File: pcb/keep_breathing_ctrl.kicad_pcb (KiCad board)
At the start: 4 copper layers, 112 x 131 mm, 177 parts, among them J2 Screw_Terminal, P1 CONN_RASPBERRY, Q1 PN2222, Q2 PN2222, U1 MPL3115A2, U10 PCF8523TK, U11 AQH3213AX, U12 AQH3213AX, U13 HTS221, U14 ICE40UP5K-SG48ITR, U15 GD25Q32CTIGR-Memory_Flash, U16 UCC12040, U17 ISO7762, U18 ZLDO1117G33TA, U19 NCP177, U2 powerSTEP01, U3 TLP240D, U4 TLP240D, U5 TLP240D, U6 TLP240D, U7 TLP240D, U8 TLP240D, U9 ZLDO1117G33TA, Y1 ABS06-107-32.768KHZ-T

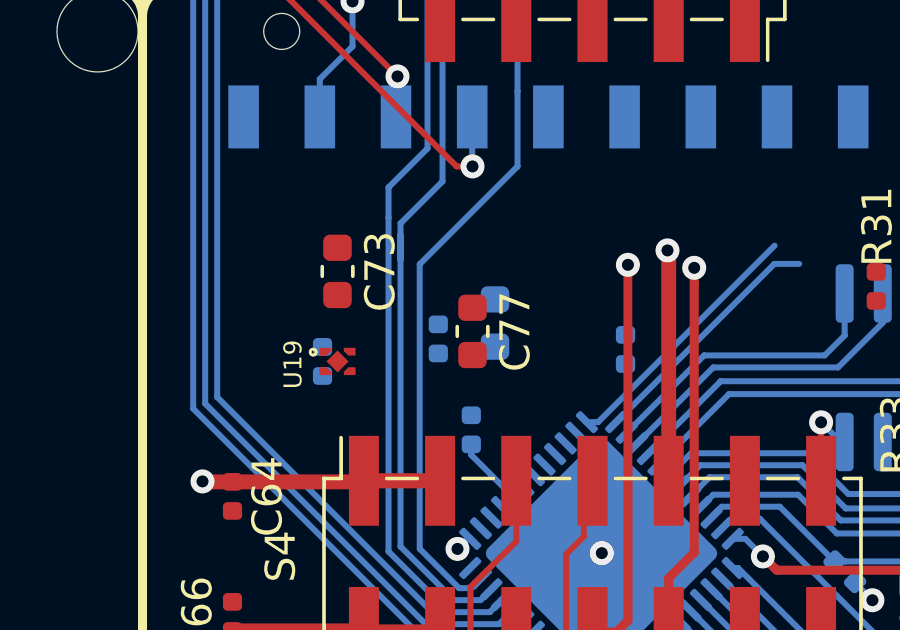
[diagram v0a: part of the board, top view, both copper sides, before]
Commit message: 1.2v ldo changed
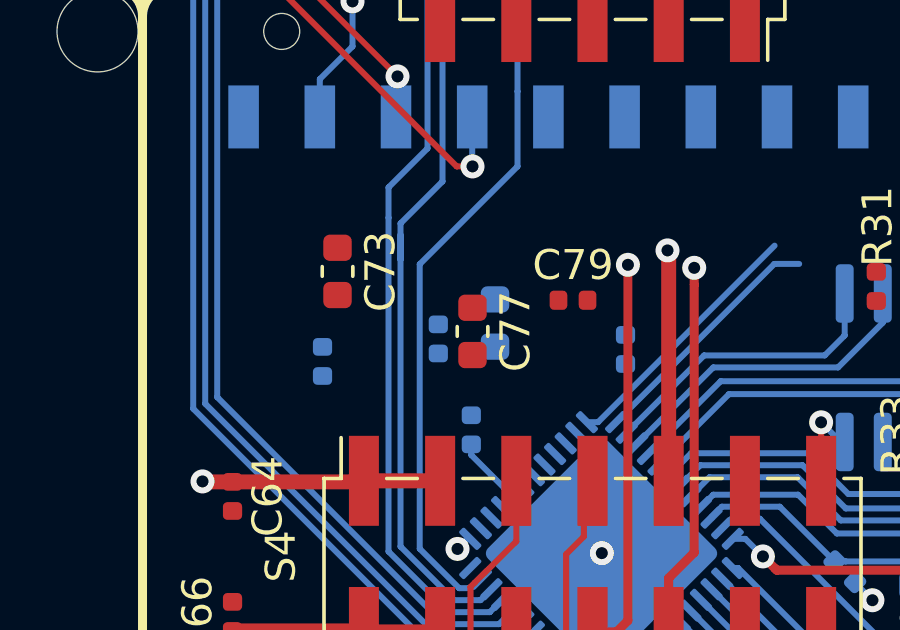
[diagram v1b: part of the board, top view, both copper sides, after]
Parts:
- removed U19: NCP177, SMD:XDFN4
- added C79: 0.1u, Capacitor_SMD:C_0402_1005Metric, F.Cu at (124.8, 113.5)
- C77: value 1uF -> 2.2uF
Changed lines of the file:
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@@
-(kicad_pcb (version 20171130) (host pcbnew 5.1.4+dfsg1-1)
+(kicad_pcb (version 20171130) (host pcbnew 5.1.5-52549c5~84~ubuntu19.04.1)
   (general
     (thickness 1.6)
@@
     (add_net /I2C/I2C_SDA)
     (add_net "/Power Stepper/M_CLK")
+    (add_net "/Power Stepper/M_CS")
     (add_net "/Power Stepper/M_MISO")
     (add_net "/Power Stepper/M_MOSI")
+    (add_net "/Power Stepper/M_RST")
     (add_net "/Power Stepper/SM_CLK")
     (add_net "/Power Stepper/SM_CS")
@@
     (add_net /Rapsberry/SPI_MOSI)
     (add_net /STM32F4/BOOT0)
+    (add_net /STM32F4/CM1B)
+    (add_net /STM32F4/CM1D)
+    (add_net /STM32F4/IO10)
+    (add_net /STM32F4/IO11)
+    (add_net /STM32F4/IO12)
+    (add_net /STM32F4/IO13)
+    (add_net /STM32F4/IO14)
+    (add_net /STM32F4/IO15)
+    (add_net /STM32F4/IO16)
+    (add_net /STM32F4/IO17)
+    (add_net /STM32F4/IO18)
+    (add_net /STM32F4/IO19)
+    (add_net /STM32F4/IO20)
+    (add_net /STM32F4/IO21)
+    (add_net /STM32F4/IO22)
+    (add_net /STM32F4/IO23)
+    (add_net /STM32F4/IO24)
+    (add_net /STM32F4/IO25)
+    (add_net /STM32F4/IO26)
+    (add_net /STM32F4/IO27)
+    (add_net /STM32F4/IO28)
+    (add_net /STM32F4/IO29)
+    (add_net /STM32F4/IO31)
+    (add_net /STM32F4/IO32)
+    (add_net /STM32F4/IO9)
+    (add_net /STM32F4/LED)
+    (add_net /STM32F4/NRESET)
     (add_net /STM32F4/PE0)
     (add_net /STM32F4/PE1)
@@
     (add_net /STM32F4/PE6)
     (add_net /STM32F4/PE7)
+    (add_net /STM32F4/RST_ESP)
+    (add_net /STM32F4/SDIO_CMD)
+    (add_net /STM32F4/SDIO_D0)
+    (add_net /STM32F4/SDIO_D1)
+    (add_net /STM32F4/STM_I2C1_SCL)
+    (add_net /STM32F4/STM_I2C1_SDA)
     (add_net /STM32F4/STM_UART_RX)
+    (add_net /STM32F4/TRIGG_3V3)
+    (add_net /STM32F4/VDDAST)
     (add_net /SensorShields/ANALOG_0)
     (add_net /SensorShields/ANALOG_1)
@@
     (add_net /SensorShields/ANALOG_7)
     (add_net /SensorShields/ANALOG_8)
+    (add_net /SensorShields/CDONE)
     (add_net /SensorShields/CRESET_N)
     (add_net /SensorShields/FPGA_SI)
@@
     (add_net /SensorShields/SPI_MISO)
     (add_net /SensorShields/SPI_MOSI)
+    (add_net /SensorShields/SS_SPI_CLK)
+    (add_net /SensorShields/SS_SPI_CS)
+    (add_net /SensorShields/SS_SPI_MISO)
+    (add_net /SensorShields/SS_SPI_MOSI)
     (add_net /SensorShields/VCC_PLL)
     (add_net /Sensors/SCL)
@@
     (add_net "Net-(C3-Pad1)")
     (add_net "Net-(C33-Pad1)")
+    (add_net "Net-(C79-Pad1)")
+    (add_net "Net-(CRT1-Pad2)")
+    (add_net "Net-(CRT2-Pad2)")
+    (add_net "Net-(CST3-Pad2)")
+    (add_net "Net-(CST4-Pad2)")
+    (add_net "Net-(CXST1-Pad1)")
+    (add_net "Net-(CXST2-Pad1)")
     (add_net "Net-(D3-Pad1)")
     (add_net "Net-(D5-Pad1)")
@@
     (add_net "Net-(D7-Pad1)")
     (add_net "Net-(D7-Pad2)")
+    (add_net "Net-(J10-Pad3)")
+    (add_net "Net-(J10-Pad4)")
+    (add_net "Net-(J11-Pad3)")
+    (add_net "Net-(J11-Pad4)")
+    (add_net "Net-(J12-Pad3)")
+    (add_net "Net-(J12-Pad4)")
     (add_net "Net-(J3-Pad1)")
     (add_net "Net-(J4-Pad1)")
+    (add_net "Net-(J7-Pad3)")
+    (add_net "Net-(J7-Pad4)")
+    (add_net "Net-(J8-Pad3)")
+    (add_net "Net-(J8-Pad4)")
+    (add_net "Net-(J9-Pad3)")
+    (add_net "Net-(J9-Pad4)")
     (add_net "Net-(JP1-Pad1)")
     (add_net "Net-(JP2-Pad1)")
     (add_net "Net-(JP4-Pad1)")
     (add_net "Net-(JP4-Pad3)")
+    (add_net "Net-(LST2-Pad2)")
+    (add_net "Net-(P1-Pad1)")
+    (add_net "Net-(P1-Pad11)")
+    (add_net "Net-(P1-Pad13)")
+    (add_net "Net-(P1-Pad15)")
+    (add_net "Net-(P1-Pad17)")
+    (add_net "Net-(P1-Pad2)")
+    (add_net "Net-(P1-Pad27)")
+    (add_net "Net-(P1-Pad28)")
+    (add_net "Net-(P1-Pad31)")
+    (add_net "Net-(P1-Pad32)")
+    (add_net "Net-(P1-Pad33)")
+    (add_net "Net-(P1-Pad35)")
+    (add_net "Net-(P1-Pad36)")
+    (add_net "Net-(P1-Pad37)")
+    (add_net "Net-(P1-Pad38)")
+    (add_net "Net-(P1-Pad4)")
+    (add_net "Net-(P1-Pad40)")
     (add_net "Net-(Q1-Pad2)")
     (add_net "Net-(Q1-Pad3)")
@@
     (add_net "Net-(R36-Pad1)")
     (add_net "Net-(R39-Pad2)")
+    (add_net "Net-(U1-Pad5)")
+    (add_net "Net-(U1-Pad6)")
+    (add_net "Net-(U11-Pad5)")
+    (add_net "Net-(U12-Pad5)")
+    (add_net "Net-(U13-Pad3)")
+    (add_net "Net-(U14-Pad2)")
+    (add_net "Net-(U14-Pad3)")
+    (add_net "Net-(U14-Pad4)")
+    (add_net "Net-(U14-Pad48)")
     (add_net "Net-(U16-Pad10)")
+    (add_net "Net-(U16-Pad4)")
+    (add_net "Net-(U16-Pad5)")
+    (add_net "Net-(U17-Pad1)")
+    (add_net "Net-(U17-Pad7)")
+    (add_net "Net-(U2-Pad63)")
+    (add_net "Net-(U2-Pad64)")
+    (add_net "Net-(UST1-Pad15)")
+    (add_net "Net-(UST1-Pad16)")
+    (add_net "Net-(UST1-Pad18)")
+    (add_net "Net-(UST1-Pad36)")
+    (add_net "Net-(UST1-Pad39)")
+    (add_net "Net-(UST1-Pad40)")
+    (add_net "Net-(UST1-Pad41)")
+    (add_net "Net-(UST1-Pad42)")
+    (add_net "Net-(UST1-Pad43)")
+    (add_net "Net-(UST1-Pad44)")
+    (add_net "Net-(UST1-Pad45)")
+    (add_net "Net-(UST1-Pad46)")
+    (add_net "Net-(UST1-Pad47)")
+    (add_net "Net-(UST1-Pad55)")
+    (add_net "Net-(UST1-Pad56)")
+    (add_net "Net-(UST1-Pad57)")
+    (add_net "Net-(UST1-Pad58)")
     (add_net OUTA1)
     (add_net OUTA2)
@@
     (add_net SM_BUSY)
     (add_net SM_FLAG)
+    (add_net SM_STCLK)
+    (add_net SM_SW)
     (add_net VMOTOR)
+  )
+  (module Capacitor_SMD:C_0402_1005Metric (layer F.Cu)
+    (at 124.85 113.46)
+    (descr "Capacitor SMD 0402 (1005 Metric), square (rectangular) end terminal, IPC_7351 nominal, (Body size source: http://www.tortai-tech.com/upload/download/2011102023233369053.pdf), generated with kicad-footprint-generator")
+    (tags capacitor)
+    (attr smd)
+    (fp_text reference C79 (at 0 -1.17) (layer F.SilkS)
+      (effects (font (size 1 1) (thickness 0.15)))
+    )
+    (fp_text value 0.1u (at 0 1.17) (layer F.Fab)
+      (effects (font (size 1 1) (thickness 0.15)))
+    )
+    (fp_text user %R (at 0 0) (layer F.Fab)
+      (effects (font (size 0.25 0.25) (thickness 0.04)))
+    )
+    (fp_line (start 0.93 0.47) (end -0.93 0.47) (layer F.CrtYd) (width 0.05))
+    (fp_line (start 0.93 -0.47) (end 0.93 0.47) (layer F.CrtYd) (width 0.05))
+    (fp_line (start -0.93 -0.47) (end 0.93 -0.47) (layer F.CrtYd) (width 0.05))
+    (fp_line (start -0.93 0.47) (end -0.93 -0.47) (layer F.CrtYd) (width 0.05))
+    (fp_line (start 0.5 0.25) (end -0.5 0.25) (layer F.Fab) (width 0.1))
+    (fp_line (start 0.5 -0.25) (end 0.5 0.25) (layer F.Fab) (width 0.1))
+    (fp_line (start -0.5 -0.25) (end 0.5 -0.25) (layer F.Fab) (width 0.1))
+    (fp_line (start -0.5 0.25) (end -0.5 -0.25) (layer F.Fab) (width 0.1))
+    (pad 2 smd roundrect (at 0.485 0) (size 0.59 0.64) (layers F.Cu F.Paste F.Mask) (roundrect_rratio 0.25)
+      (net 1 GND))
+    (pad 1 smd roundrect (at -0.485 0) (size 0.59 0.64) (layers F.Cu F.Paste F.Mask) (roundrect_rratio 0.25))
+    (model ${KISYS3DMOD}/Capacitor_SMD.3dshapes/C_0402_1005Metric.wrl
+      (at (xyz 0 0 0))
+      (scale (xyz 1 1 1))
+      (rotate (xyz 0 0 0))
+    )
   )
   (module Capacitor_SMD:C_0603_1608Metric (layer F.Cu)
@@
       (effects (font (size 1 1) (thickness 0.15)))
     )
-    (fp_text value 1uF (at 0 1.43 90) (layer F.Fab)
+    (fp_text value 2.2uF (at 0 1.43 90) (layer F.Fab)
       (effects (font (size 1 1) (thickness 0.15)))
     )
@@
     )
   )
-  (module SMD:XDFN4 (layer F.Cu)
-    (at 117 115.5 270)
-    (fp_text reference U19 (at 0.1 1.48 90) (layer F.SilkS)
-      (effects (font (size 0.6 0.6) (thickness 0.15)))
-    )
-    (fp_text value NCP177 (at 0.38 -2.78 90) (layer F.Fab)
-      (effects (font (size 1 1) (thickness 0.15)))
-    )
-    (fp_circle (center -0.31 0.81) (end -0.21 0.81) (layer F.SilkS) (width 0.1))
-    (pad 4 smd custom (at -0.325 -0.405 90) (size 0.1 0.1) (layers F.Cu F.Paste F.Mask)
-      (net 73 +3V3) (zone_connect 0)
-      (options (clearance outline) (anchor rect))
-      (primitives
-        (gr_poly (pts
-           (xy -0.13 0.195) (xy 0.13 0.195) (xy 0.13 -0.195) (xy 0.02 -0.195) (xy -0.13 -0.045)
-) (width 0))
-      ))
-    (pad EPAD smd rect (at 0 0 315) (size 0.52 0.52) (layers F.Cu F.Paste F.Mask)
-      (net 1 GND))
-    (pad 2 smd custom (at 0.325 0.405 270) (size 0.1 0.1) (layers F.Cu F.Paste F.Mask)
-      (net 1 GND) (zone_connect 0)
-      (options (clearance outline) (anchor rect))
-      (primitives
-        (gr_poly (pts
-           (xy -0.13 0.195) (xy 0.13 0.195) (xy 0.13 -0.195) (xy 0.02 -0.195) (xy -0.13 -0.045)
-) (width 0))
-      ))
-    (pad 3 smd custom (at 0.325 -0.405 90) (size 0.1 0.1) (layers F.Cu F.Paste F.Mask)
-      (net 73 +3V3) (zone_connect 0)
-      (options (clearance outline) (anchor rect))
-      (primitives
-        (gr_poly (pts
-           (xy -0.13 0.195) (xy -0.13 -0.195) (xy -0.02 -0.195) (xy 0.13 -0.045) (xy 0.13 0.195)
-) (width 0))
-      ))
-    (pad 1 smd custom (at -0.325 0.405 270) (size 0.1 0.1) (layers F.Cu F.Paste F.Mask)
-      (net 121 1V2_ICE) (zone_connect 0)
-      (options (clearance outline) (anchor rect))
-      (primitives
-        (gr_poly (pts
-           (xy -0.13 0.195) (xy -0.13 -0.195) (xy -0.02 -0.195) (xy 0.13 -0.045) (xy 0.13 0.195)
-) (width 0))
-      ))
-  )
   (module Capacitor_SMD:C_0402_1005Metric (layer B.Cu)

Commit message: routing....
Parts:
- C50: footprint Resistor_SMD:R_0402_1005Metric -> Resistor_SMD:R_0603_1608Metric
- R29, R5: footprint Resistor_SMD:R_0603_1608Metric -> Resistor_SMD:R_0402_1005Metric; moved to F.Cu
- R32, R33, R34: footprint Resistor_SMD:R_0603_1608Metric -> Resistor_SMD:R_0402_1005Metric
- R41: moved to B.Cu
- moved R41 24.3 mm to (125.2, 111.6), turned to 90 degrees
- moved R5 12.9 mm to (143.9, 104.8), turned to 180 degrees
- moved R29 9.11 mm to (139.9, 104.8), turned to 180 degrees
- moved R31 5.46 mm to (140.4, 113.0)
- moved C50 2.45 mm to (130.6, 130.2), turned to 0 degrees
- moved C48 2.01 mm to (131.4, 128.0)
- moved R37 1.98 mm to (135.4, 111.2)
- moved C46 1.46 mm to (130.6, 132.4), turned to 0 degrees
- moved R38 1.42 mm to (140.9, 110.9), turned to 180 degrees
- moved R33 1.13 mm to (138.1, 118.5)
- moved R28 1.12 mm to (138.1, 109.7)
- moved C42 0.86 mm to (121.5, 116.9)
- moved R40 0.55 mm to (142.1, 104.5)
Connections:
- C79 pad 1: (no net) -> +3V3
- P1 pad 11: (no net) -> /Rapsberry/RST_ICE
- P1 pad 29: /Rapsberry/RST_ICE -> (no net)
- U14 pad 2: (no net) -> /SensorShields/SPI_MISO
- U14 pad 3: (no net) -> /SensorShields/I2C_SDA_4
- U14 pad 39: /SensorShields/I2C_SDA_4 -> /SensorShields/SPI_CLK
- U14 pad 4: (no net) -> /SensorShields/I2C_CLK_4
- U14 pad 40: /SensorShields/I2C_CLK_4 -> /SensorShields/SPI_MOSI
- U14 pad 41: /SensorShields/SPI_CS_4 -> (no net)
- U14 pad 48: (no net) -> /SensorShields/SPI_CS_4
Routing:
- net /SensorShields/I2C_SDA_2: track 8.29 -> 48.2 mm, vias 0 -> 1
- net /SensorShields/I2C_CLK_2: track 8.69 -> 47.7 mm, vias 0 -> 1
- net /SensorShields/FT_SSn: track 12.8 -> 33.2 mm, vias 0 -> 1
- net 1V2_ICE: track 5.92 -> 19.7 mm, vias 1 -> 2
- net GND: track 18.6 -> 31.7 mm, vias 8 -> 14
- net 3V3_M: track 30.6 -> 18.4 mm, vias 2 -> 1
- net /SensorShields/FT_SCK: track 10.8 -> 22.4 mm, vias 0 -> 1
- net /SensorShields/SPI_MOSI: track 259.4 -> 270.7 mm
- net +3V3: track 101.2 -> 110.7 mm, vias 16 -> 20
- net /SensorShields/FPGA_SI: track 10.9 -> 19.7 mm, vias 0 -> 1
- net /SensorShields/SPI_CLK: track 266.6 -> 259.9 mm
- net /SensorShields/I2C_CLK_4: track 10.9 -> 4.67 mm
- net /SensorShields/SPI_MISO: track 266.6 -> 272.5 mm, vias 11 -> 12
- net Net-(R33-Pad1): track 0.00 -> 5.67 mm, vias 0 -> 1
- net /Rapsberry/SPI_MOSI: track 0.00 -> 4.02 mm, vias 0 -> 1
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
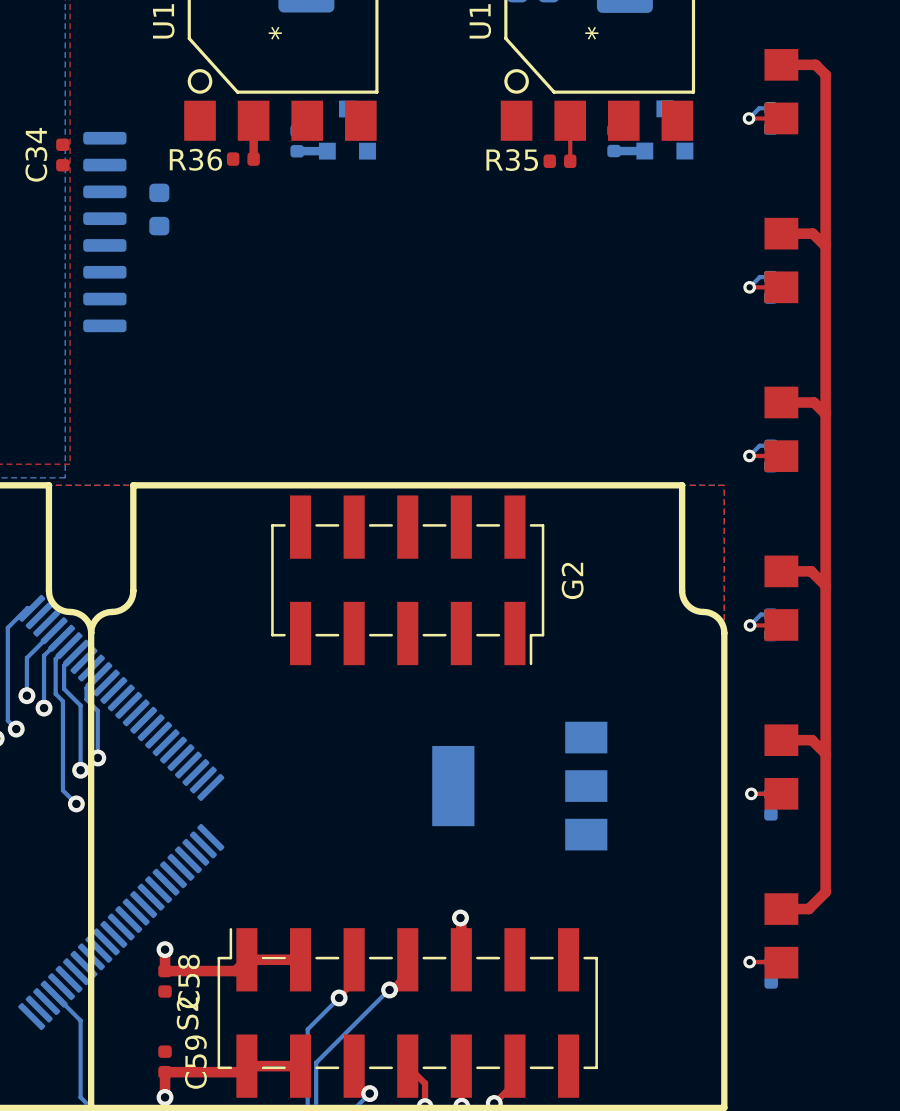
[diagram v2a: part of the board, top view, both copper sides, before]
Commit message: solid state stm32's signals connected
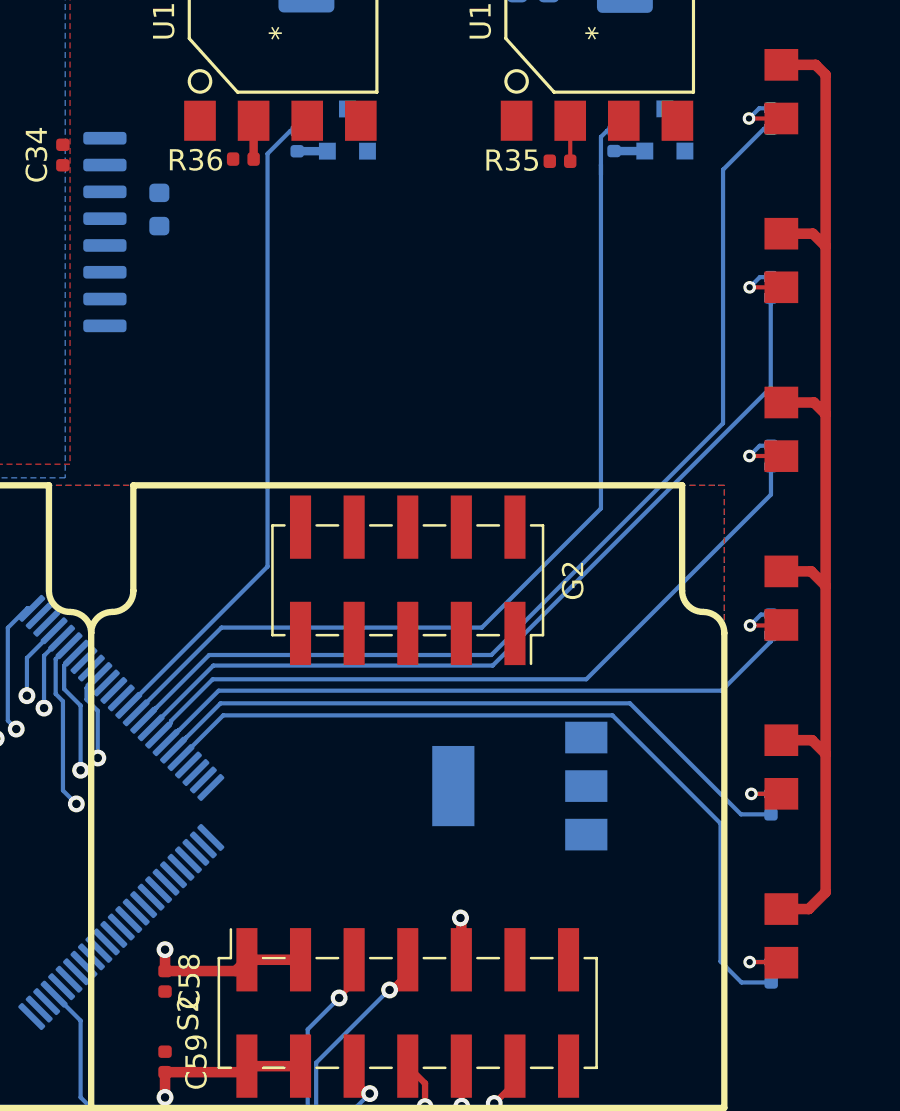
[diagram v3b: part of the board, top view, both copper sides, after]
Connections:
- UST1 pad 1: /STM32F4/PE2 -> (no net)
- UST1 pad 2: /STM32F4/PE3 -> (no net)
- UST1 pad 3: /STM32F4/PE4 -> (no net)
- UST1 pad 38: /STM32F4/PE7 -> (no net)
- UST1 pad 39: (no net) -> /STM32F4/PE7
- UST1 pad 4: /STM32F4/PE5 -> (no net)
- UST1 pad 40: (no net) -> /STM32F4/PE6
- UST1 pad 41: (no net) -> /STM32F4/PE5
- UST1 pad 42: (no net) -> /STM32F4/PE4
- UST1 pad 43: (no net) -> /STM32F4/PE3
- UST1 pad 44: (no net) -> /STM32F4/PE2
- UST1 pad 45: (no net) -> /STM32F4/PE1
- UST1 pad 46: (no net) -> /STM32F4/PE0
- UST1 pad 5: /STM32F4/PE6 -> (no net)
- UST1 pad 97: /STM32F4/PE0 -> (no net)
- UST1 pad 98: /STM32F4/PE1 -> (no net)
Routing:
- net /STM32F4/PE5: track 0.00 -> 48.4 mm
- net /STM32F4/PE6: track 0.00 -> 44.8 mm
- net /STM32F4/PE4: track 0.00 -> 40.3 mm
- net /STM32F4/PE0: track 0.01 -> 37.9 mm
- net /STM32F4/PE3: track 0.00 -> 35.1 mm
- net /STM32F4/PE1: track 0.00 -> 31.4 mm
- net /STM32F4/PE2: track 0.00 -> 30.9 mm
- net /STM32F4/PE7: track 0.00 -> 30.7 mm
